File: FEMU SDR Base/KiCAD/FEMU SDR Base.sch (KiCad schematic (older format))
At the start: 43 parts, among them P1 Battery, P10 PWM_In_2, P11 PWM_In_3, P12 PWM_In_4, P13 PWM_Out_1, P14 PWM_Out_2, P15 PWM_Out_2, P16 PWM_Out_2, P17 SDR_1_USB, P18 SDR_2_USB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

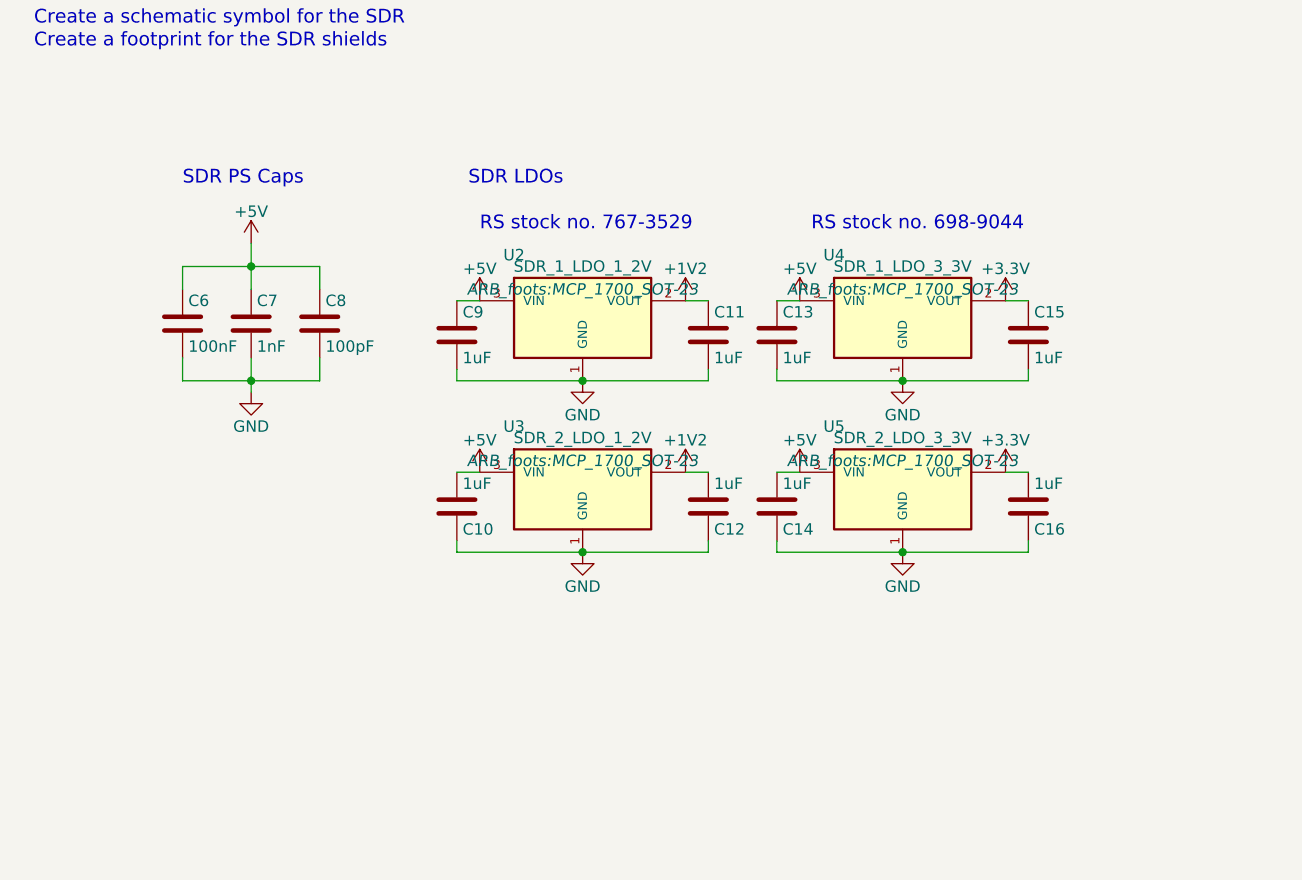
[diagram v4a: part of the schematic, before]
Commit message: added SDR LDO components and edited RasPi PSU shield footprint
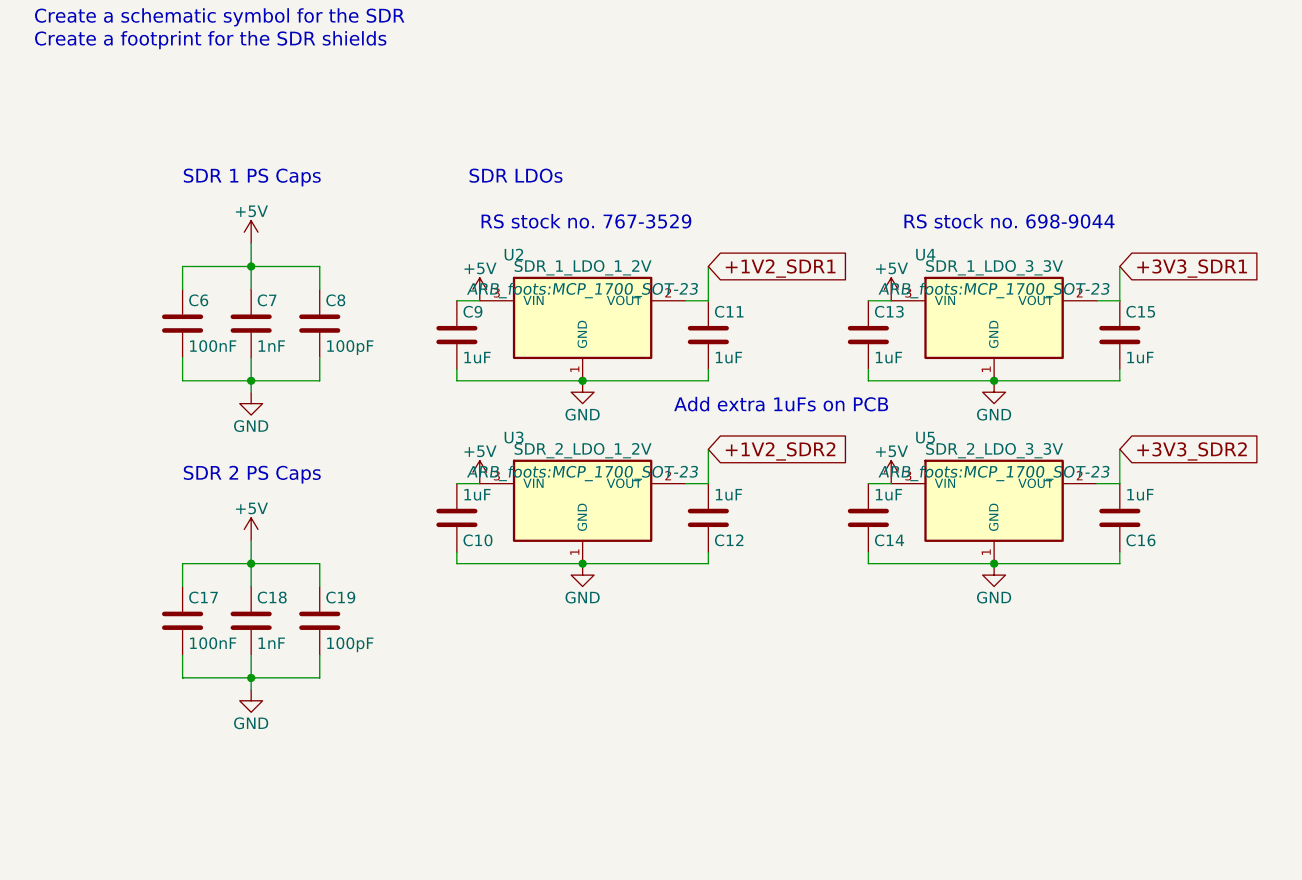
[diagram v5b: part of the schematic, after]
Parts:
- added C17: 100nF, Capacitors_SMD:C_0805_HandSoldering, symbol C
- added C18: 1nF, Capacitors_SMD:C_0805_HandSoldering, symbol C
- added C19: 100pF, Capacitors_SMD:C_0805_HandSoldering, symbol C
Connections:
- net +5V: now also C17.1, C18.1, C19.1
- net GND: now also C17.2, C18.2, C19.2
- net +1V2 renamed +1V2_SDR1
- net +1V2_SDR1: no longer C12.2, U3.2 (VOUT)
- net +3V3 renamed +3V3_SDR1
- net +3V3_SDR1: no longer C16.2, U5.2 (VOUT)
- new net +1V2_SDR2: C12.2, U3.2 (VOUT)
- new net +3V3_SDR2: C16.2, U5.2 (VOUT)
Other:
- note added: "Add extra 1uFs on PCB"
- note added: "SDR 1 PS Caps"
- note added: "SDR 2 PS Caps"
- note removed: "SDR PS Caps"
- moved on the sheet: C10, C12, C13, C14, C15, C16, U3, U4, U5

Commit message: Base schematic edit
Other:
- note added: "SDR Shield\nRS Components Stock No.: 627-6455"
- moved on the sheet: P2, P3, P8
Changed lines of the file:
@@
 L CONN_01X01 P2
 U 1 1 57224F5B
-P 1150 4800
-F 0 "P2" H 1150 4900 50  0000 C CNN
-F 1 "SDR_Shield_1" V 1250 4800 50  0000 C CNN
-F 2 "" H 1150 4800 50  0001 C CNN
-F 3 "" H 1150 4800 50  0000 C CNN
-	1    1150 4800
+P 1100 4900
+F 0 "P2" H 1100 5000 50  0000 C CNN
+F 1 "SDR_Shield_1" V 1200 4900 50  0000 C CNN
+F 2 "" H 1100 4900 50  0001 C CNN
+F 3 "" H 1100 4900 50  0000 C CNN
+	1    1100 4900
 	0    -1   -1   0
 $EndComp
@@
 L CONN_01X01 P3
 U 1 1 57225014
-P 1750 4800
-F 0 "P3" H 1750 4900 50  0000 C CNN
-F 1 "SDR_Shield_2" V 1850 4800 50  0000 C CNN
-F 2 "" H 1750 4800 50  0001 C CNN
-F 3 "" H 1750 4800 50  0000 C CNN
-	1    1750 4800
+P 1700 4900
+F 0 "P3" H 1700 5000 50  0000 C CNN
+F 1 "SDR_Shield_2" V 1800 4900 50  0000 C CNN
+F 2 "" H 1700 4900 50  0001 C CNN
+F 3 "" H 1700 4900 50  0000 C CNN
+	1    1700 4900
 	0    -1   -1   0
 $EndComp
@@
 L CONN_01X01 P8
 U 1 1 572250B6
-P 2450 4800
-F 0 "P8" H 2450 4900 50  0000 C CNN
-F 1 "Raspi_Power_Shield" V 2550 4800 50  0000 C CNN
-F 2 "ARB_foots:PCB_Shield_29x25mm" H 2450 4800 50  0001 C CNN
-F 3 "" H 2450 4800 50  0000 C CNN
-	1    2450 4800
+P 2400 4900
+F 0 "P8" H 2400 5000 50  0000 C CNN
+F 1 "Raspi_Power_Shield" V 2500 4900 50  0000 C CNN
+F 2 "ARB_foots:PCB_Shield_29x25mm" H 2400 4900 50  0001 C CNN
+F 3 "" H 2400 4900 50  0000 C CNN
+	1    2400 4900
 	0    -1   -1   0
 $EndComp
@@
 L GND #PWR06
 U 1 1 572251A0
-P 1150 5100
-F 0 "#PWR06" H 1150 4850 50  0001 C CNN
-F 1 "GND" H 1150 4950 50  0000 C CNN
-F 2 "" H 1150 5100 50  0000 C CNN
-F 3 "" H 1150 5100 50  0000 C CNN
-	1    1150 5100
+P 1100 5200
+F 0 "#PWR06" H 1100 4950 50  0001 C CNN
+F 1 "GND" H 1100 5050 50  0000 C CNN
+F 2 "" H 1100 5200 50  0000 C CNN
+F 3 "" H 1100 5200 50  0000 C CNN
+	1    1100 5200
 	1    0    0    -1
 $EndComp
@@
 L GND #PWR07
 U 1 1 57225200
-P 1750 5100
-F 0 "#PWR07" H 1750 4850 50  0001 C CNN
-F 1 "GND" H 1750 4950 50  0000 C CNN
-F 2 "" H 1750 5100 50  0000 C CNN
-F 3 "" H 1750 5100 50  0000 C CNN
-	1    1750 5100
+P 1700 5200
+F 0 "#PWR07" H 1700 4950 50  0001 C CNN
+F 1 "GND" H 1700 5050 50  0000 C CNN
+F 2 "" H 1700 5200 50  0000 C CNN
+F 3 "" H 1700 5200 50  0000 C CNN
+	1    1700 5200
 	1    0    0    -1
 $EndComp
@@
 L GND #PWR08
 U 1 1 57225259
-P 2450 5100
-F 0 "#PWR08" H 2450 4850 50  0001 C CNN
-F 1 "GND" H 2450 4950 50  0000 C CNN
-F 2 "" H 2450 5100 50  0000 C CNN
-F 3 "" H 2450 5100 50  0000 C CNN
-	1    2450 5100
+P 2400 5200
+F 0 "#PWR08" H 2400 4950 50  0001 C CNN
+F 1 "GND" H 2400 5050 50  0000 C CNN
+F 2 "" H 2400 5200 50  0000 C CNN
+F 3 "" H 2400 5200 50  0000 C CNN
+	1    2400 5200
 	1    0    0    -1
 $EndComp
@@
 	2900 4050 3300 4050
 Wire Wire Line
-	1150 5000 1150 5100
-Wire Wire Line
-	1750 5000 1750 5100
-Wire Wire Line
-	2450 5000 2450 5100
+	1100 5100 1100 5200
+Wire Wire Line
+	1700 5100 1700 5200
+Wire Wire Line
+	2400 5100 2400 5200
 Wire Wire Line
 	6150 3100 6150 3200
@@
 Text Notes 8300 3350 0    60   ~ 0
 Add extra 1uFs on PCB
+Text Notes 850  5600 0    60   ~ 0
+SDR Shield\nRS Components Stock No.: 627-6455
 $EndSCHEMATC

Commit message: Added SDR shield footprint, updated raspi shield footprints
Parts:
- P2, P3: footprint (none) -> ARB_foots:SDR_Shield_75x50mm
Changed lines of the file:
@@
 F 0 "P2" H 1100 5000 50  0000 C CNN
 F 1 "SDR_Shield_1" V 1200 4900 50  0000 C CNN
-F 2 "" H 1100 4900 50  0001 C CNN
+F 2 "ARB_foots:SDR_Shield_75x50mm" H 1100 4900 50  0001 C CNN
 F 3 "" H 1100 4900 50  0000 C CNN
 	1    1100 4900
@@
 F 0 "P3" H 1700 5000 50  0000 C CNN
 F 1 "SDR_Shield_2" V 1800 4900 50  0000 C CNN
-F 2 "" H 1700 4900 50  0001 C CNN
+F 2 "ARB_foots:SDR_Shield_75x50mm" H 1700 4900 50  0001 C CNN
 F 3 "" H 1700 4900 50  0000 C CNN
 	1    1700 4900

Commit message: Planning and review
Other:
- note added: "Add Main Power Connector"
- note added: "Add connection for raspberry pi power\n"
- note removed: "Add 1.2V LDO power"
- note removed: "Add 3.3V LDO power for sdr\n"
- note removed: "Add sdr power supply capacitors\n"
- note removed: "Create a footprint for the SDR shields"
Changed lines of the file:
@@
 Text Notes 1350 4600 0    60   ~ 0
 Shield grounding\n
-Text Notes 5500 1050 0    60   ~ 0
-Add sdr power supply capacitors\n
 Text Notes 5500 1150 0    60   ~ 0
 Add sdr oscilator - SKIP for now (no XOs available)
-Text Notes 5500 1250 0    60   ~ 0
-Add 3.3V LDO power for sdr\n
-Text Notes 5500 1350 0    60   ~ 0
-Add 1.2V LDO power
 Text Notes 5500 1450 0    60   ~ 0
 Add feed through capacitors for incomming 5V power rail (Not in schematic)
@@
 Text Notes 4400 2450 0    60   ~ 0
 SDR USB distribution\n\n
-Text Notes 5500 1650 0    60   ~ 0
-Create a schematic symbol for the SDR
 $Comp
 L C C6
@@
 Wire Wire Line
 	10250 3650 10150 3650
-Text Notes 5500 1750 0    60   ~ 0
-Create a footprint for the SDR shields
 $Comp
 L C C17
@@
 Text Notes 850  5600 0    60   ~ 0
 SDR Shield\nRS Components Stock No.: 627-6455
+Text Notes 5500 1650 0    60   ~ 0
+Create a schematic symbol for the SDR
+Text Notes 5500 1300 0    60   ~ 0
+Add Main Power Connector
+Text Notes 5500 1750 0    60   ~ 0
+Add connection for raspberry pi power\n
 $EndSCHEMATC
